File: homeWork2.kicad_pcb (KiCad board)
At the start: 2 copper layers, 125 x 99.9 mm, 43 parts, among them J1 Barrel_Jack_Switch_SMT, U1 LM7805_TO220

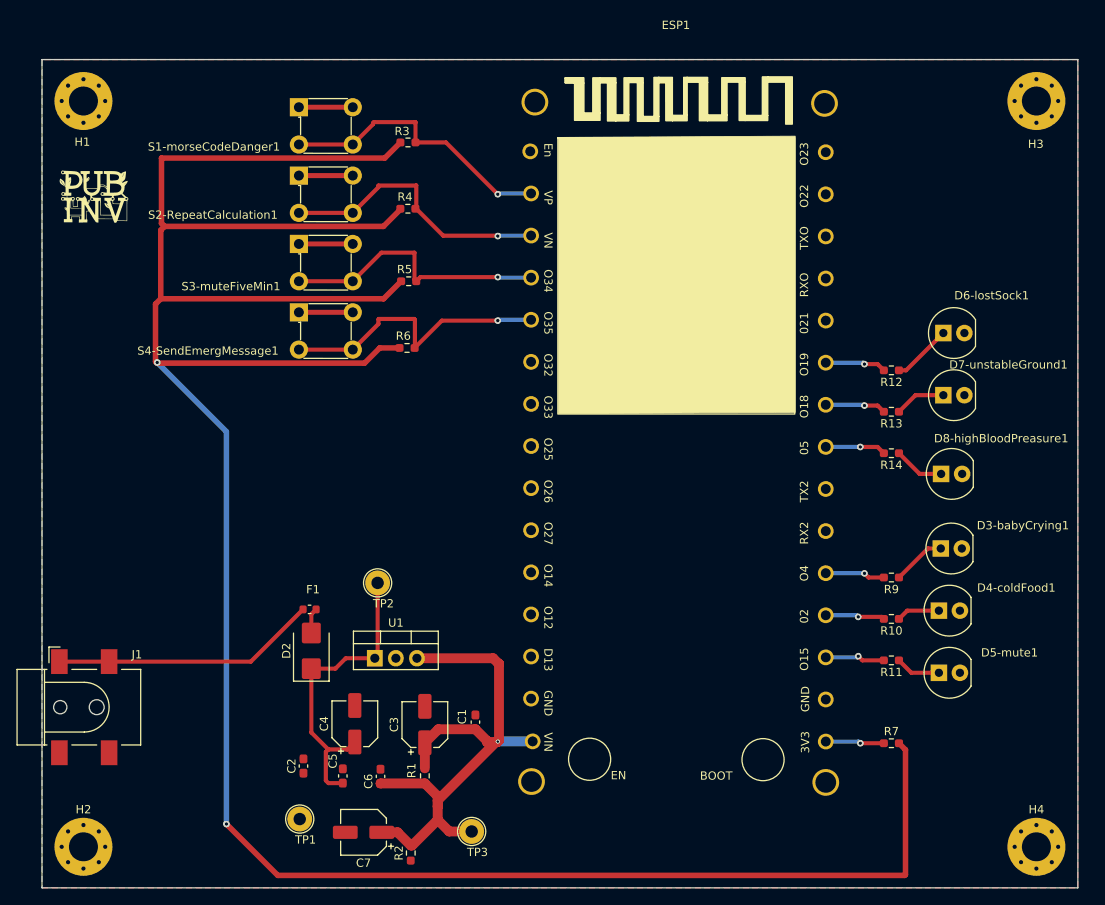
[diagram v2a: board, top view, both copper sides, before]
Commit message: Changed the style of routing, the connections are the same.
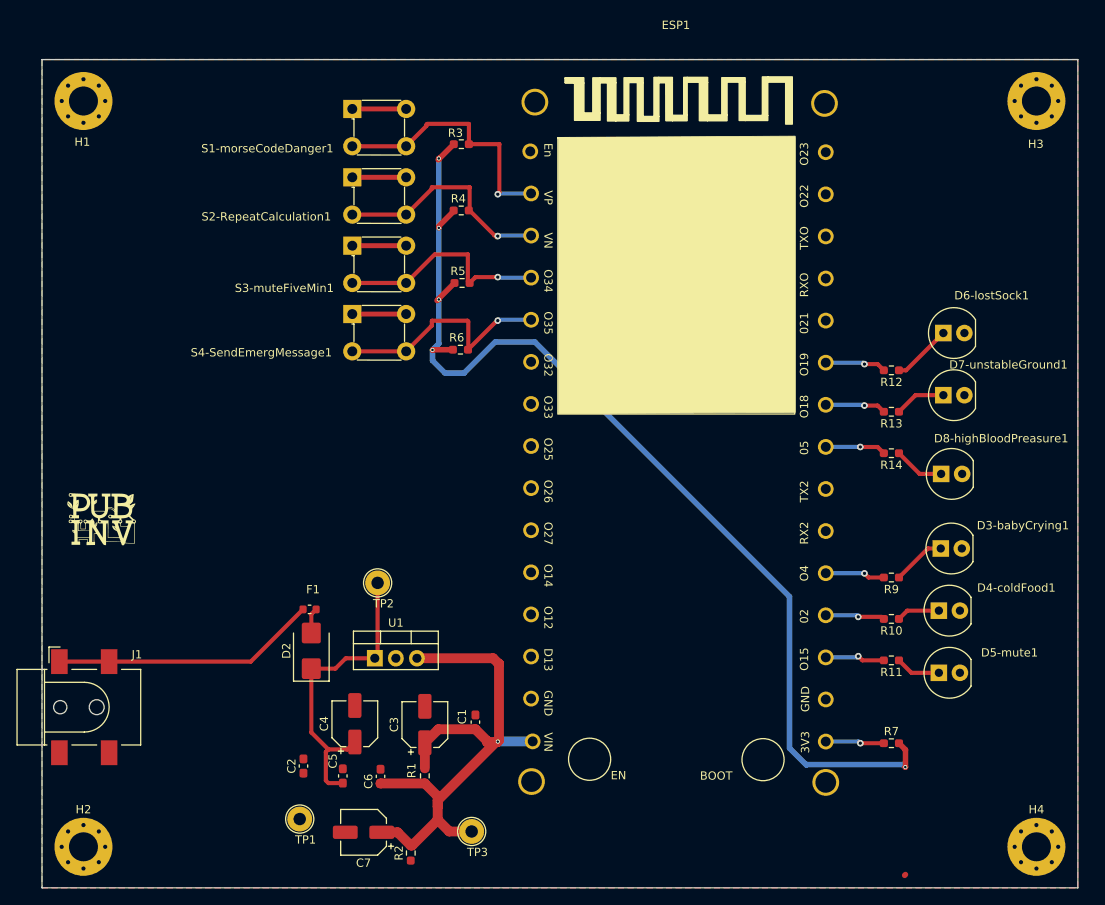
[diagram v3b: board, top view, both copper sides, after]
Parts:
- moved G*** 38.9 mm to (57.2, 105.7)
- moved R3 6.44 mm to (100.6, 60.2)
- moved R5 6.44 mm to (100.7, 77.0)
- moved R6 6.44 mm to (100.5, 85.0)
- moved S1-morseCodeDanger1 6.44 mm to (87.4, 56.0)
- moved S2-RepeatCalculation1 6.44 mm to (87.4, 64.2)
- moved S3-muteFiveMin1 6.44 mm to (87.4, 72.5)
- moved S4-SendEmergMessage1 6.44 mm to (87.4, 80.7)
- moved R4 6.44 mm to (100.6, 68.2)
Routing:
- net +3.3V: track 304.1 -> 130.4 mm, vias 2 -> 5
- net Net-(ESP1-O35): track 34.8 -> 28.0 mm
- net Net-(ESP1-O34): track 33.0 -> 26.7 mm
- net Net-(ESP1-VN): track 33.7 -> 27.6 mm
- net Net-(ESP1-VP): track 34.3 -> 31.6 mm

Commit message: Added Bill of material and Parts list.
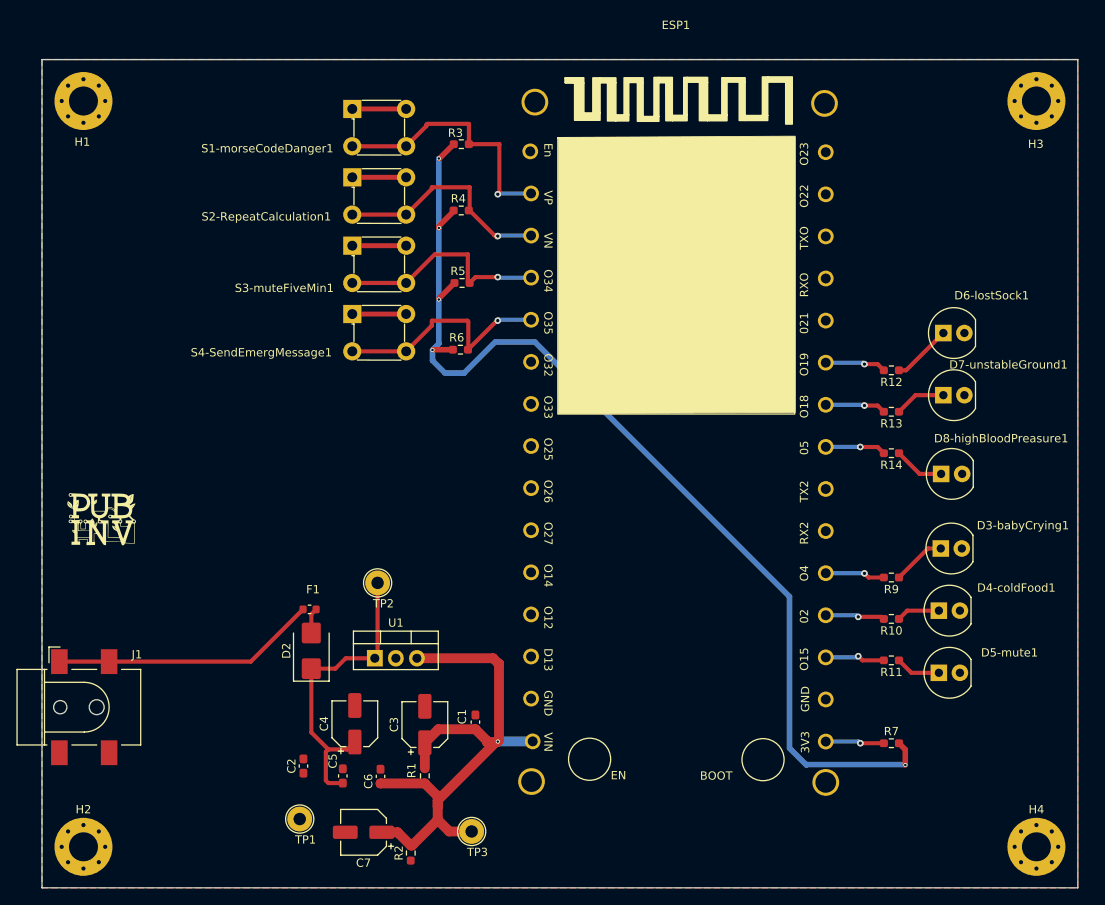
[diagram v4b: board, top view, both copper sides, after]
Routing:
- net +3.3V: track 130.4 -> 129.0 mm
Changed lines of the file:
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@@
     (pcbplotparams
       (layerselection 0x00010fc_ffffffff)
-      (plot_on_all_layers_selection 0x0000000_00000000)
+      (plot_on_all_layers_selection 0x0001000_00000000)
       (disableapertmacros false)
       (usegerberextensions false)
@@
       (outputformat 1)
       (mirror false)
-      (drillshape 1)
+      (drillshape 0)
       (scaleselection 1)
-      (outputdirectory "")
+      (outputdirectory "Gerbers/")
     )
   )
@@
   (segment (start 105.093 66.157) (end 105 66.25) (width 0.5) (layer "B.Cu") (net 20))
   (segment (start 97.8815 70.1055) (end 97.8815 70.312) (width 0.67) (layer "F.Cu") (net 21))
-  (segment (start 154.2 133.2875) (end 153.4125 132.5) (width 0.67) (layer "F.Cu") (net 21))
-  (segment (start 97.664 79.073) (end 97.789 78.948) (width 0.67) (layer "F.Cu") (net 21))
-  (segment (start 97.1555 85.044) (end 97.1195 85.044) (width 0.67) (layer "F.Cu") (net 21))
-  (segment (start 97.789 78.948) (end 97.8815 78.948) (width 0.67) (layer "F.Cu") (net 21))
-  (segment (start 97.8815 61.93) (end 97.8815 62.018) (width 0.67) (layer "F.Cu") (net 21))
-  (segment (start 154.178 135.382) (end 154.2 135.36) (width 0.67) (layer "F.Cu") (net 21))
-  (segment (start 154.2 135.36) (end 154.2 133.2875) (width 0.67) (layer "F.Cu") (net 21))
-  (segment (start 154.2 135.404) (end 154.178 135.382) (width 0.67) (layer "F.Cu") (net 21))
+  (segment (start 154.178 135.128) (end 154.178 133.2655) (width 0.67) (layer "F.Cu") (net 21))
   (segment (start 97.8815 78.8555) (end 99.779 76.958) (width 0.67) (layer "F.Cu") (net 21))
-  (segment (start 97.9695 61.93) (end 97.8815 61.93) (width 0.67) (layer "F.Cu") (net 21))
-  (segment (start 97.1915 85.008) (end 97.1555 85.044) (width 0.67) (layer "F.Cu") (net 21))
-  (segment (start 97.8815 78.948) (end 97.8815 78.8555) (width 0.67) (layer "F.Cu") (net 21))
+  (segment (start 154.178 133.2655) (end 153.4125 132.5) (width 0.67) (layer "F.Cu") (net 21))
   (segment (start 99.6915 60.208) (end 97.9695 61.93) (width 0.67) (layer "F.Cu") (net 21))
   (segment (start 99.679 68.308) (end 97.8815 70.1055) (width 0.67) (layer "F.Cu") (net 21))
   (segment (start 99.579 85.008) (end 97.1915 85.008) (width 0.67) (layer "F.Cu") (net 21))
-  (segment (start 97.8815 62.018) (end 97.8065 62.093) (width 0.67) (layer "F.Cu") (net 21))
-  (segment (start 97.1195 85.044) (end 97.1195 85.08) (width 0.67) (layer "F.Cu") (net 21))
-  (segment (start 154.1 148.45) (end 154.2 148.35) (width 0.67) (layer "F.Cu") (net 21))
   (via (at 97.8815 70.312) (size 0.5) (drill 0.3) (layers "F.Cu" "B.Cu") (net 21))
   (via (at 97.8815 61.93) (size 0.5) (drill 0.3) (layers "F.Cu" "B.Cu") (net 21))
   (via (at 97.1195 85.044) (size 0.5) (drill 0.3) (layers "F.Cu" "B.Cu") (net 21))
-  (via (at 154.178 135.382) (size 0.5) (drill 0.3) (layers "F.Cu" "B.Cu") (net 21))
+  (via (at 154.178 135.128) (size 0.5) (drill 0.3) (layers "F.Cu" "B.Cu") (net 21))
   (via (at 97.8815 78.948) (size 0.5) (drill 0.3) (layers "F.Cu" "B.Cu") (net 21))
+  (segment (start 142.24 135.128) (end 142.291249 135.076751) (width 0.67) (layer "B.Cu") (net 21))
+  (segment (start 97.1195 86.314) (end 98.6435 87.838) (width 0.67) (layer "B.Cu") (net 21))
+  (segment (start 142.291249 135.076751) (end 154.178 135.076751) (width 0.67) (layer "B.Cu") (net 21))
+  (segment (start 97.1195 85.044) (end 97.1195 86.314) (width 0.67) (layer "B.Cu") (net 21))
+  (segment (start 104.6935 84.074) (end 109.474 84.074) (width 0.67) (layer "B.Cu") (net 21))
   (segment (start 109.474 84.074) (end 140.208 114.808) (width 0.67) (layer "B.Cu") (net 21))
-  (segment (start 140.208 114.808) (end 140.208 133.096) (width 0.67) (layer "B.Cu") (net 21))
-  (segment (start 100.9295 87.838) (end 104.6935 84.074) (width 0.67) (layer "B.Cu") (net 21))
   (segment (start 97.8815 78.948) (end 97.8815 84.282) (width 0.67) (layer "B.Cu") (net 21))
-  (segment (start 142.24 135.128) (end 142.291249 135.076751) (width 0.67) (layer "B.Cu") (net 21))
   (segment (start 97.8815 61.93) (end 97.8815 70.312) (width 0.67) (layer "B.Cu") (net 21))
-  (segment (start 153.872751 135.076751) (end 154.178 135.382) (width 0.67) (layer "B.Cu") (net 21))
-  (segment (start 97.1195 85.044) (end 97.1195 86.314) (width 0.67) (layer "B.Cu") (net 21))
+  (segment (start 140.208 114.808) (end 140.208 133.096) (width 0.67) (layer "B.Cu") (net 21))
   (segment (start 98.6435 87.838) (end 100.9295 87.838) (width 0.67) (layer "B.Cu") (net 21))
-  (segment (start 97.1195 86.314) (end 98.6435 87.838) (width 0.67) (layer "B.Cu") (net 21))
-  (segment (start 142.291249 135.076751) (end 153.872751 135.076751) (width 0.67) (layer "B.Cu") (net 21))
-  (segment (start 97.8815 70.312) (end 97.8815 78.948) (width 0.67) (layer "B.Cu") (net 21))
-  (segment (start 104.6935 84.074) (end 109.474 84.074) (width 0.67) (layer "B.Cu") (net 21))
+  (segment (start 100.9295 87.838) (end 104.6935 84.074) (width 0.67) (layer "B.Cu") (net 21))
   (segment (start 140.208 133.096) (end 142.24 135.128) (width 0.67) (layer "B.Cu") (net 21))
+  (segment (start 97.8815 70.312) (end 97.8815 78.948) (width 0.67) (layer "B.Cu") (net 21))
   (segment (start 97.8815 84.282) (end 97.1195 85.044) (width 0.67) (layer "B.Cu") (net 21))
   (segment (start 104.582 71.186) (end 101.604 68.208) (width 0.5) (layer "F.Cu") (net 22))

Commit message: Gerber files and enhancements file are added,
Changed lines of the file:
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@@
     (pts (xy 50 150) (xy 170 150))
     (height 10)
-    (gr_text "120.0000 mm" (at 110 158.85) (layer "Dwgs.User")
+    (gr_text "4724.4094 mils" (at 110 158.85) (layer "Dwgs.User")
       (effects (font (size 1 1) (thickness 0.15)))
     )
@@
     (pts (xy 175 50) (xy 50 50))
     (height 10)
-    (gr_text "125.0000 mm" (at 112.5 38.85) (layer "Dwgs.User")
+    (gr_text "4921.2598 mils" (at 112.5 38.85) (layer "Dwgs.User")
       (effects (font (size 1 1) (thickness 0.15)))
     )
@@
     (pts (xy 50 150) (xy 50 128))
     (height -7)
-    (gr_text "22.0000 mm" (at 41.85 139 90) (layer "Dwgs.User")
+    (gr_text "866.1417 mils" (at 41.85 139 90) (layer "Dwgs.User")
       (effects (font (size 1 1) (thickness 0.15)))
     )
@@
     (pts (xy 50 50) (xy 50 150))
     (height 11)
-    (gr_text "100.0000 mm" (at 37.85 100 90) (layer "Dwgs.User")
+    (gr_text "3937.0079 mils" (at 37.85 100 90) (layer "Dwgs.User")
       (effects (font (size 1 1) (thickness 0.15)))
     )
@@
     (pts (xy 50 150) (xy 50 55))
     (height -9)
-    (gr_text "95.0000 mm" (at 39.85 102.5 90) (layer "Dwgs.User")
+    (gr_text "3740.1575 mils" (at 39.85 102.5 90) (layer "Dwgs.User")
       (effects (font (size 1 1) (thickness 0.15)))
     )
@@
     (pts (xy 50 150) (xy 50 145))
     (height -4)
-    (gr_text "5.0000 mm" (at 44.85 147.5 90) (layer "Dwgs.User")
+    (gr_text "196.8504 mils" (at 44.85 147.5 90) (layer "Dwgs.User")
       (effects (font (size 1 1) (thickness 0.15)))
     )
@@
     (pts (xy 47 128) (xy 50 128))
     (height 14)
-    (gr_text "3.0000 mm" (at 48.5 140.85) (layer "Dwgs.User")
+    (gr_text "118.1102 mils" (at 48.5 140.85) (layer "Dwgs.User")
       (effects (font (size 1 1) (thickness 0.15)))
     )
@@
   (segment (start 97.75 140.15) (end 97.75 138.9) (width 1.19) (layer "F.Cu") (net 3))
   (segment (start 103.7 132.2125) (end 103.7 132.35) (width 1.19) (layer "F.Cu") (net 3))
-  (segment (start 97.75 139.4) (end 97.75 140.15) (width 1.19) (layer "F.Cu") (net 3))
   (segment (start 91 143.25) (end 92.9125 143.25) (width 1.19) (layer "F.Cu") (net 3))
   (segment (start 96.2 137.35) (end 90.8625 137.35) (width 1.19) (layer "F.Cu") (net 3))
@@
   (segment (start 105.1 122.9) (end 105.15 122.9) (width 1.19) (layer "F.Cu") (net 3))
   (segment (start 97.75 138.9) (end 96.2 137.35) (width 1.19) (layer "F.Cu") (net 3))
+  (segment (start 104.85 132.3) (end 97.75 139.4) (width 1.19) (layer "F.Cu") (net 3))
   (segment (start 94.5 144.8375) (end 94.6625 144.8375) (width 1.19) (layer "F.Cu") (net 3))
+  (segment (start 105 132.3) (end 104.85 132.3) (width 1.19) (layer "F.Cu") (net 3))
   (segment (start 105.15 122.9) (end 105.15 122.95) (width 1.19) (layer "F.Cu") (net 3))
   (segment (start 95.24 122.245) (end 104.445 122.245) (width 1.19) (layer "F.Cu") (net 3))
+  (segment (start 105 132.3) (end 104.95 132.35) (width 1.19) (layer "F.Cu") (net 3))
+  (segment (start 105 132.3) (end 105.15 132.15) (width 1.19) (layer "F.Cu") (net 3))
   (segment (start 105.15 122.95) (end 105.05 122.85) (width 1.19) (layer "F.Cu") (net 3))
   (segment (start 97.75 141.75) (end 99.15 143.15) (width 1.19) (layer "F.Cu") (net 3))
@@
   (segment (start 103.7 132.35) (end 103.8375 132.35) (width 1.19) (layer "F.Cu") (net 3))
   (segment (start 104.445 122.245) (end 105.1 122.9) (width 1.19) (layer "F.Cu") (net 3))
-  (segment (start 105 132.3) (end 104.95 132.35) (width 1.19) (layer "F.Cu") (net 3))
-  (segment (start 104.85 132.3) (end 97.75 139.4) (width 1.19) (layer "F.Cu") (net 3))
   (segment (start 97.8375 130.8125) (end 96.2 132.45) (width 1.19) (layer "F.Cu") (net 3))
+  (segment (start 97.75 139.4) (end 97.75 140.15) (width 1.19) (layer "F.Cu") (net 3))
   (segment (start 104.95 132.35) (end 103.7 132.35) (width 1.19) (layer "F.Cu") (net 3))
-  (segment (start 105 132.3) (end 105.15 132.15) (width 1.19) (layer "F.Cu") (net 3))
   (segment (start 97.75 141.75) (end 97.75 140.15) (width 1.19) (layer "F.Cu") (net 3))
   (segment (start 96.2 132.45) (end 96.2 135.525) (width 1.19) (layer "F.Cu") (net 3))
   (segment (start 99.15 143.15) (end 101.85 143.15) (width 1.19) (layer "F.Cu") (net 3))
-  (segment (start 105 132.3) (end 104.85 132.3) (width 1.19) (layer "F.Cu") (net 3))
   (segment (start 105.15 132.15) (end 105.15 122.95) (width 1.19) (layer "F.Cu") (net 3))
-  (via (at 105 132.3) (size 0.5) (drill 0.3) (layers "F.Cu" "B.Cu") (net 3))
-  (segment (start 105.023 132.277) (end 105 132.3) (width 1.19) (layer "B.Cu") (net 3))
-  (segment (start 109.2107 132.277) (end 105.023 132.277) (width 1.19) (layer "B.Cu") (net 3))
+  (via (at 105 132.3) (size 1.5) (drill 0.5) (layers "F.Cu" "B.Cu") (net 3))
+  (segment (start 105.023 132.277) (end 109.2107 132.277) (width 1.19) (layer "B.Cu") (net 3))
+  (segment (start 105 132.3) (end 105.023 132.277) (width 1.19) (layer "B.Cu") (net 3))
   (segment (start 82.5 119.2) (end 82.5 116.925) (width 0.5) (layer "F.Cu") (net 5))
   (segment (start 82.5 116.925) (end 83.075 116.35) (width 0.5) (layer "F.Cu") (net 5))
@@
   (segment (start 99.679 68.308) (end 97.8815 70.1055) (width 0.67) (layer "F.Cu") (net 21))
   (segment (start 99.579 85.008) (end 97.1915 85.008) (width 0.67) (layer "F.Cu") (net 21))
-  (via (at 97.8815 70.312) (size 0.5) (drill 0.3) (layers "F.Cu" "B.Cu") (net 21))
-  (via (at 97.8815 61.93) (size 0.5) (drill 0.3) (layers "F.Cu" "B.Cu") (net 21))
-  (via (at 97.1195 85.044) (size 0.5) (drill 0.3) (layers "F.Cu" "B.Cu") (net 21))
-  (via (at 154.178 135.128) (size 0.5) (drill 0.3) (layers "F.Cu" "B.Cu") (net 21))
-  (via (at 97.8815 78.948) (size 0.5) (drill 0.3) (layers "F.Cu" "B.Cu") (net 21))
+  (via (at 97.8815 70.312) (size 1.3) (drill 0.6) (layers "F.Cu" "B.Cu") (net 21))
+  (via (at 97.8815 61.93) (size 1.3) (drill 0.6) (layers "F.Cu" "B.Cu") (net 21))
+  (via (at 97.1195 85.044) (size 1.3) (drill 0.6) (layers "F.Cu" "B.Cu") (net 21))
+  (via (at 154.178 135.128) (size 1.3) (drill 0.6) (layers "F.Cu" "B.Cu") (net 21))
+  (via (at 97.8815 78.948) (size 1.3) (drill 0.6) (layers "F.Cu" "B.Cu") (net 21))
   (segment (start 142.24 135.128) (end 142.291249 135.076751) (width 0.67) (layer "B.Cu") (net 21))
   (segment (start 97.1195 86.314) (end 98.6435 87.838) (width 0.67) (layer "B.Cu") (net 21))

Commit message: updates to the pcb and the schematics.
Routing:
- added copper zone on B.Cu, net GND
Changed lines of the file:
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@@
+    )
+  )
+  (zone (net 1) (net_name "GND") (layer "B.Cu") (hatch edge 0.5)
+    (connect_pads thru_hole_only (clearance 0))
+    (min_thickness 0.25) (filled_areas_thickness no)
+    (fill yes (thermal_gap 0.5) (thermal_bridge_width 0.5))
+    (polygon
+      (pts
+        (xy 175 50)
+        (xy 50.05 50)
+        (xy 50 50.05)
+        (xy 50 149.95)
+        (xy 174.95 149.95)
+        (xy 175 149.9)
+      )
     )
   )
